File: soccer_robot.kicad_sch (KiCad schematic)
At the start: 0 parts

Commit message: Started on motor control portion of schematics
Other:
- added sheet Motor Control (motor_control.kicad_sch)
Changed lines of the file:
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@@
+	)
+	(sheet
+		(at 113.03 40.64)
+		(size 35.56 34.29)
+		(exclude_from_sim no)
+		(in_bom yes)
+		(on_board yes)
+		(dnp no)
+		(fields_autoplaced yes)
+		(stroke
+			(width 0.1524)
+			(type solid)
+		)
+		(fill
+			(color 0 0 0 0)
+		)
+		(property "Sheetname" "Motor Control"
+			(at 113.03 39.9284 0)
+			(show_name no)
+			(do_not_autoplace no)
+			(effects
+				(font
+					(size 1.27 1.27)
+				)
+				(justify left bottom)
+			)
+		)
+		(property "Sheetfile" "motor_control.kicad_sch"
+			(at 113.03 75.5146 0)
+			(show_name no)
+			(do_not_autoplace no)
+			(effects
+				(font
+					(size 1.27 1.27)
+				)
+				(justify left top)
+			)
+		)
+		(instances
+			(project "soccer_robot"
+				(path "/5d6beef2-927d-465e-9043-e130f6ad5fa9"
+					(page "3")
+				)
+			)
+		)
 	)
 	(sheet

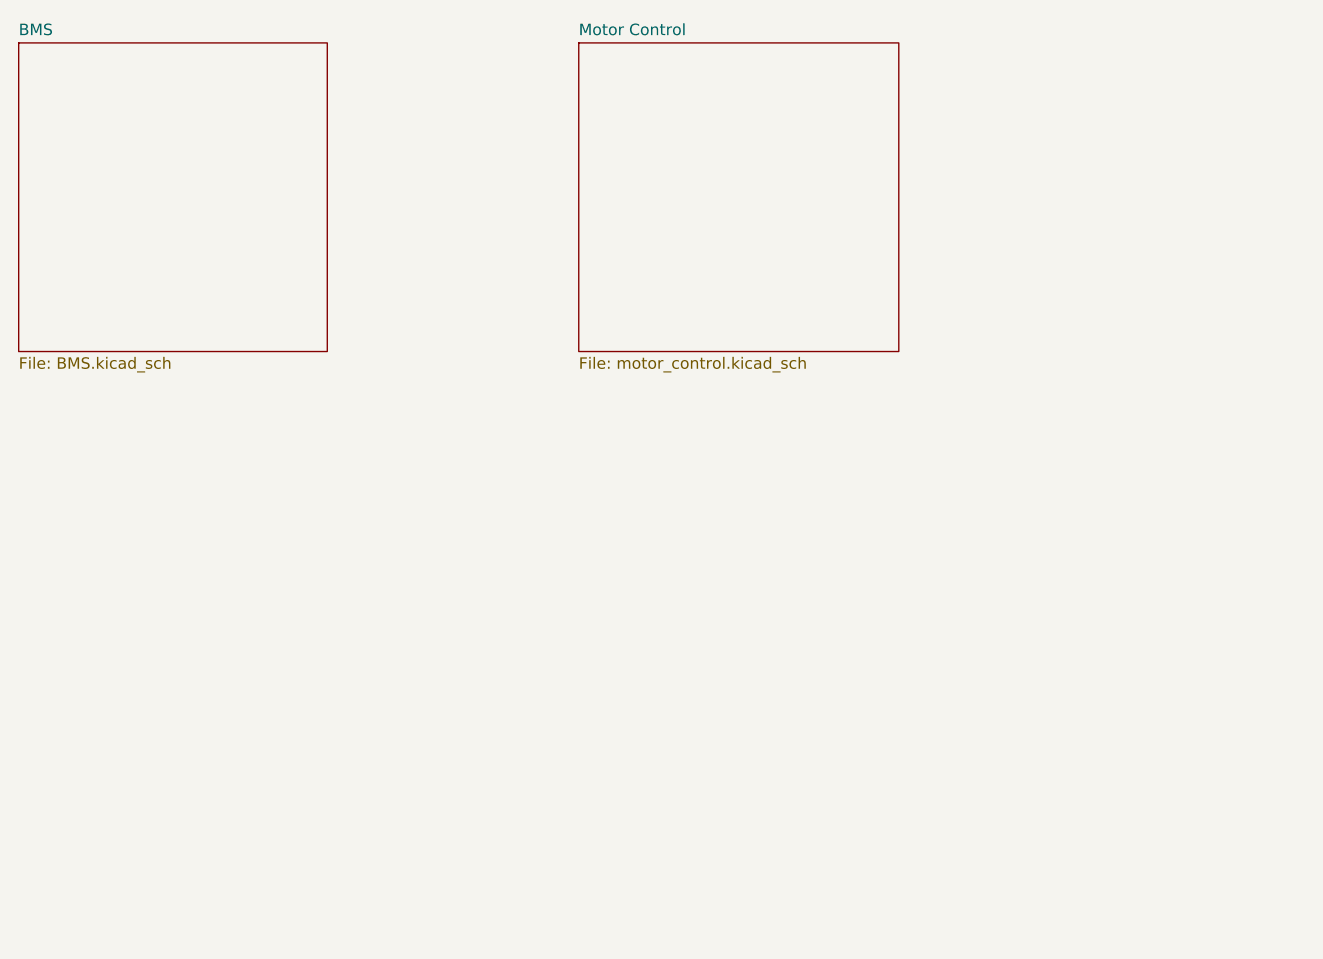
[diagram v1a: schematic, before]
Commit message: Finalized charger detection circuit, designed voltage monitor circuit, added pogo connector, finalized motor driver connections, added ESP32 connections
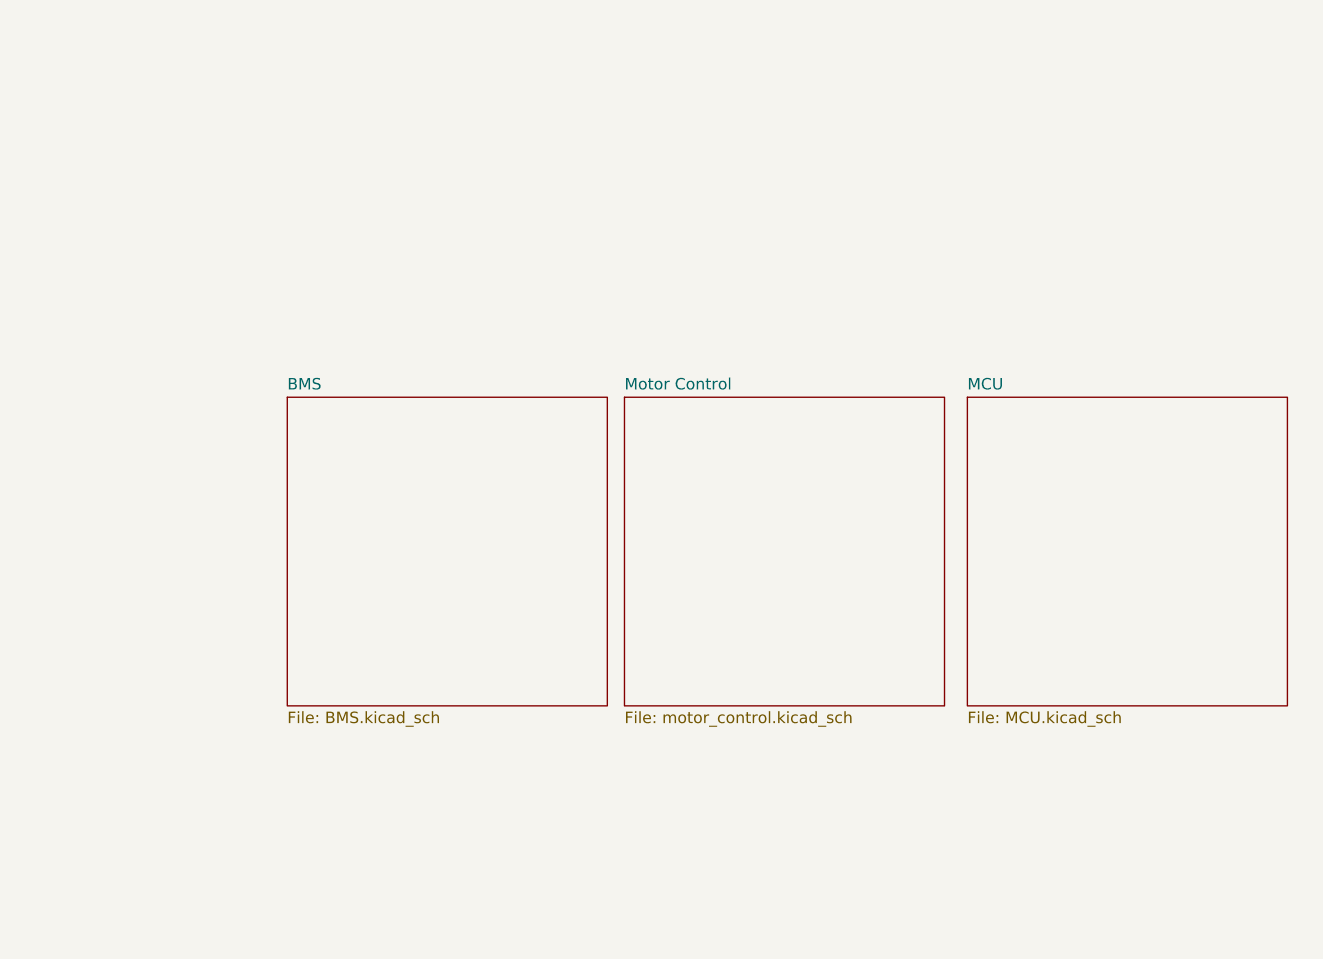
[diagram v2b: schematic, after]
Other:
- added sheet MCU (MCU.kicad_sch)
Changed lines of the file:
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@@
 	)
 	(sheet
-		(at 113.03 40.64)
+		(at 118.11 80.01)
 		(size 35.56 34.29)
 		(exclude_from_sim no)
@@
 		)
 		(property "Sheetname" "Motor Control"
-			(at 113.03 39.9284 0)
+			(at 118.11 79.2984 0)
 			(show_name no)
 			(do_not_autoplace no)
@@
 		)
 		(property "Sheetfile" "motor_control.kicad_sch"
-			(at 113.03 75.5146 0)
+			(at 118.11 114.8846 0)
 			(show_name no)
 			(do_not_autoplace no)
@@
 	)
 	(sheet
-		(at 50.8 40.64)
-		(size 34.29 34.29)
+		(at 80.645 80.01)
+		(size 35.56 34.29)
 		(exclude_from_sim no)
 		(in_bom yes)
@@
 		)
 		(property "Sheetname" "BMS"
-			(at 50.8 39.9284 0)
+			(at 80.645 79.2984 0)
 			(show_name no)
 			(do_not_autoplace no)
@@
 		)
 		(property "Sheetfile" "BMS.kicad_sch"
-			(at 50.8 75.5146 0)
+			(at 80.645 114.8846 0)
 			(show_name no)
 			(do_not_autoplace no)
@@
 				)
 			)
+		)
+	)
+	(sheet
+		(at 156.21 80.01)
+		(size 35.56 34.29)
+		(exclude_from_sim no)
+		(in_bom yes)
+		(on_board yes)
+		(dnp no)
+		(fields_autoplaced yes)
+		(stroke
+			(width 0.1524)
+			(type solid)
+		)
+		(fill
+			(color 0 0 0 0)
+		)
+		(property "Sheetname" "MCU"
+			(at 156.21 79.2984 0)
+			(show_name no)
+			(do_not_autoplace no)
+			(effects
+				(font
+					(size 1.27 1.27)
+				)
+				(justify left bottom)
+			)
+		)
+		(property "Sheetfile" "MCU.kicad_sch"
+			(at 156.21 114.8846 0)
+			(show_name no)
+			(do_not_autoplace no)
+			(effects
+				(font
+					(size 1.27 1.27)
+				)
+				(justify left top)
+			)
+		)
+		(instances
+			(project "soccer_robot"
+				(path "/5d6beef2-927d-465e-9043-e130f6ad5fa9"
+					(page "4")
+				)
+			)

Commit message: MCU buck converter design added
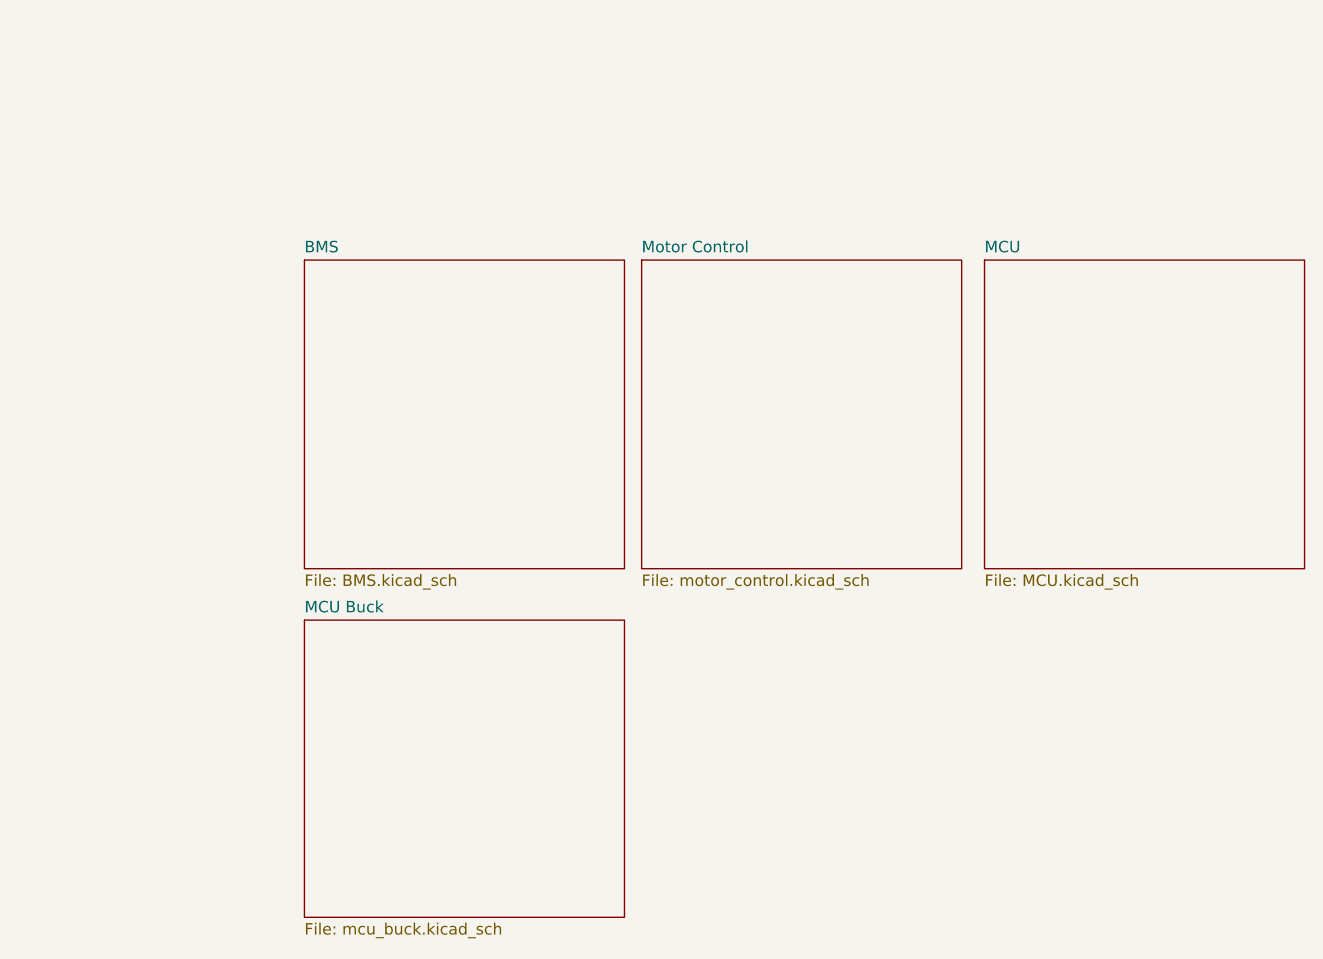
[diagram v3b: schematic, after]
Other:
- added sheet MCU Buck (mcu_buck.kicad_sch)
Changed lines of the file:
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@@
 	)
 	(sheet
-		(at 118.11 80.01)
+		(at 120.015 64.77)
 		(size 35.56 34.29)
 		(exclude_from_sim no)
@@
 		)
 		(property "Sheetname" "Motor Control"
-			(at 118.11 79.2984 0)
+			(at 120.015 64.0584 0)
 			(show_name no)
 			(do_not_autoplace no)
@@
 		)
 		(property "Sheetfile" "motor_control.kicad_sch"
-			(at 118.11 114.8846 0)
+			(at 120.015 99.6446 0)
 			(show_name no)
 			(do_not_autoplace no)
@@
 	)
 	(sheet
-		(at 80.645 80.01)
+		(at 82.55 64.77)
 		(size 35.56 34.29)
 		(exclude_from_sim no)
@@
 		)
 		(property "Sheetname" "BMS"
-			(at 80.645 79.2984 0)
+			(at 82.55 64.0584 0)
 			(show_name no)
 			(do_not_autoplace no)
@@
 		)
 		(property "Sheetfile" "BMS.kicad_sch"
-			(at 80.645 114.8846 0)
+			(at 82.55 99.6446 0)
 			(show_name no)
 			(do_not_autoplace no)
@@
 	)
 	(sheet
-		(at 156.21 80.01)
+		(at 82.55 104.775)
+		(size 35.56 33.02)
+		(exclude_from_sim no)
+		(in_bom yes)
+		(on_board yes)
+		(dnp no)
+		(fields_autoplaced yes)
+		(stroke
+			(width 0.1524)
+			(type solid)
+		)
+		(fill
+			(color 0 0 0 0)
+		)
+		(property "Sheetname" "MCU Buck"
+			(at 82.55 104.0634 0)
+			(show_name no)
+			(do_not_autoplace no)
+			(effects
+				(font
+					(size 1.27 1.27)
+				)
+				(justify left bottom)
+			)
+		)
+		(property "Sheetfile" "mcu_buck.kicad_sch"
+			(at 82.55 138.3796 0)
+			(show_name no)
+			(do_not_autoplace no)
+			(effects
+				(font
+					(size 1.27 1.27)
+				)
+				(justify left top)
+			)
+		)
+		(instances
+			(project "soccer_robot"
+				(path "/5d6beef2-927d-465e-9043-e130f6ad5fa9"
+					(page "5")
+				)
+			)
+		)
+	)
+	(sheet
+		(at 158.115 64.77)
 		(size 35.56 34.29)
 		(exclude_from_sim no)
@@
 		)
 		(property "Sheetname" "MCU"
-			(at 156.21 79.2984 0)
+			(at 158.115 64.0584 0)
 			(show_name no)
 			(do_not_autoplace no)
@@
 		)
 		(property "Sheetfile" "MCU.kicad_sch"
-			(at 156.21 114.8846 0)
+			(at 158.115 99.6446 0)
 			(show_name no)
 			(do_not_autoplace no)
